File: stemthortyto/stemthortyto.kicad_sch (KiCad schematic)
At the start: 61 parts, among them IC1 E22-900M22S, Q1 BCV29, U2 ADXL343, U3 RK3588S, U4 K4UCE3Q4AB-MGCL, U5 FEMDRW032G-88A19

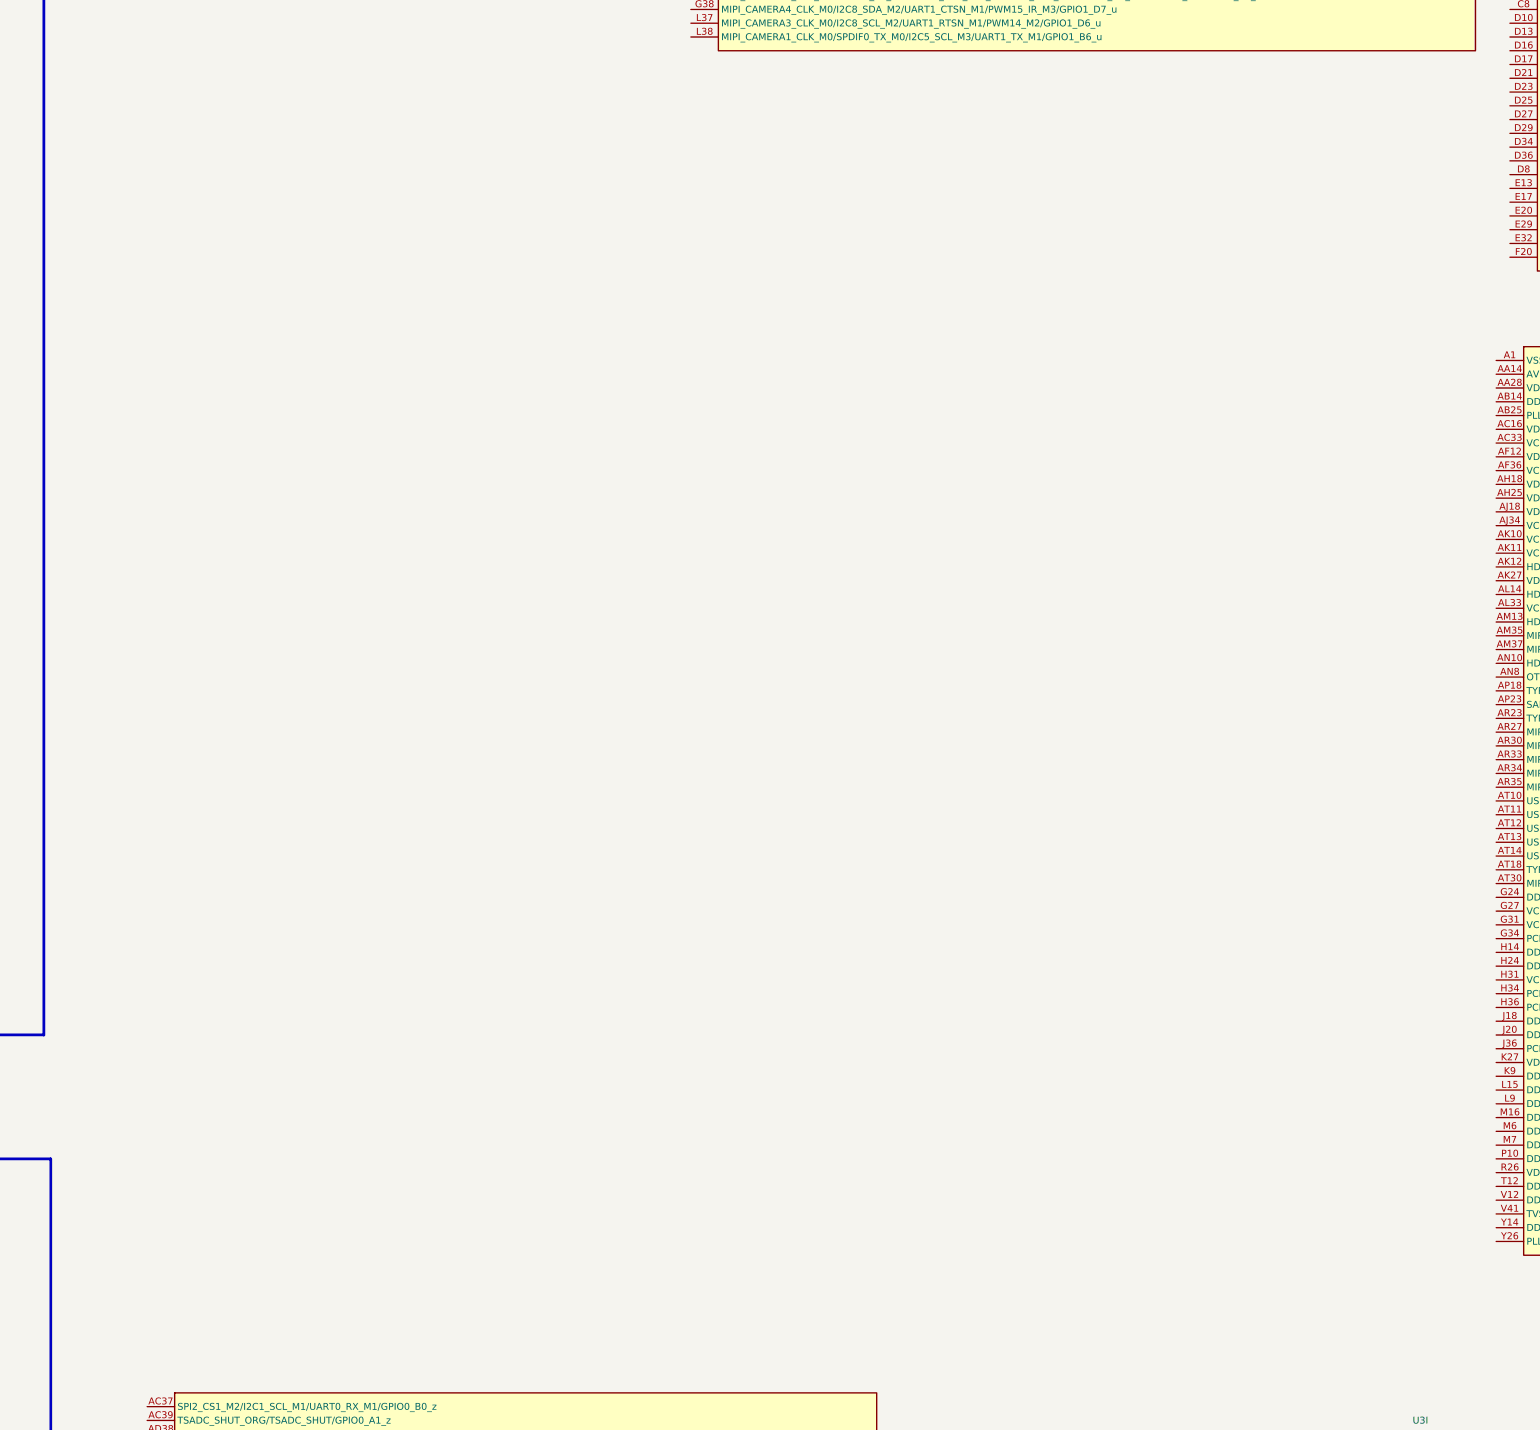
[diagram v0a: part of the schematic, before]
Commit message: Pwr.rout.comp.formmcddr, curr. using a barrel jack
Updated the board so that the power bus is ready for LPDDR and the eMMC is connected fully. Currently using a TO package linear regulator 3.3V@7.2A The eMMC data traces have also been length matched to +-4mm from each other, seeing as we're operating that at low R/W speeds anyway, shouldn't be a problem and is an upgrade from +-12mm.
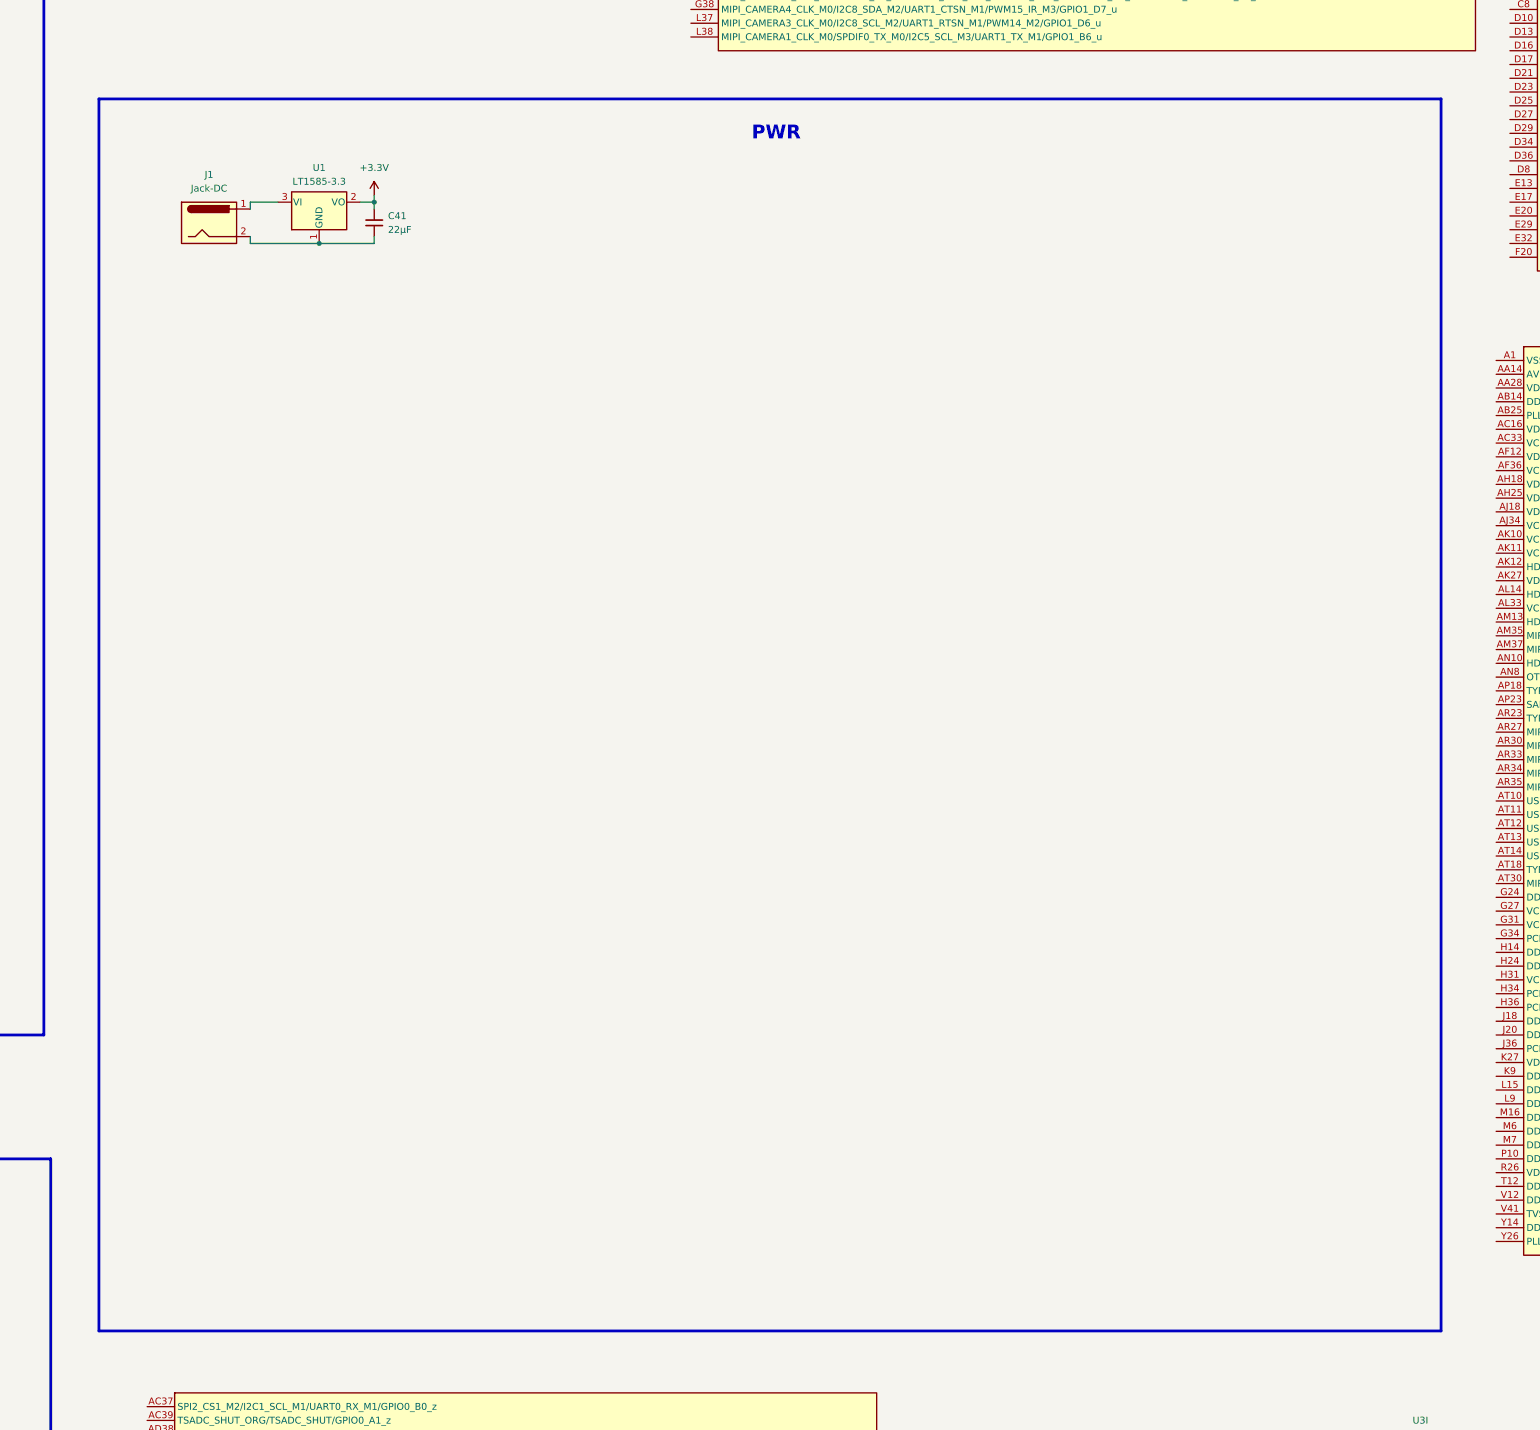
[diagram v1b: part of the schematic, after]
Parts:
- added C41: 22μF, Capacitor_SMD:C_1206_3216Metric, symbol Device:C_Small
- added J1: Jack-DC, Connector_BarrelJack:BarrelJack_Kycon_KLDX-0202-xC_Horizontal, symbol Connector:Jack-DC
- added U1: LT1585-3.3, Package_TO_SOT_THT:TO-220-3_Vertical, symbol Regulator_Linear:LT1585-3.3
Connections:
- net +3.3V: now also C41.1, U1.2 (VO)
- new net: C41.2, J1.2, U1.1 (GND)
- new net: J1.1, U1.3 (VI)
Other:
- note added: "PWR"
